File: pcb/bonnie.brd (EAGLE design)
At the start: 26.4 x 24.9 mm, 16 parts, among them J1 USB-MICROB, U1 MCP73831, U2 RT9013-XXXB

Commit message: fix: incorrect led oritentation
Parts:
- turned D3 to 0 degrees
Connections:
- net N$5: now also D3.C; no longer D3.A
- net VBUS: now also D3.A; no longer D3.C
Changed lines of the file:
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@@
 <attribute name="PROD_ID" value="RES-08295" x="46.355" y="40.005" size="1.778" layer="27" rot="R180" display="off"/>
 </element>
-<element name="D3" library="SparkFun-LED" package="LED-1206" value="RED" x="41.91" y="40.005" smashed="yes" rot="R180">
-<attribute name="PROD_ID" value="DIO-09912" x="41.91" y="40.005" size="1.778" layer="27" rot="R180" display="off"/>
-<attribute name="VALUE" x="42.926" y="41.783" size="0.4064" layer="27" rot="R180"/>
+<element name="D3" library="SparkFun-LED" package="LED-1206" value="RED" x="41.91" y="40.005" smashed="yes">
+<attribute name="PROD_ID" value="DIO-09912" x="41.91" y="40.005" size="1.778" layer="27" display="off"/>
+<attribute name="VALUE" x="40.894" y="38.227" size="0.4064" layer="27"/>
 </element>
 <element name="U2" library="v-reg-new" package="SOT23-5" value="RT9013-XXXB" x="34.925" y="36.195" smashed="yes">
@@
 <contactref element="U1" pad="4"/>
 <contactref element="C1" pad="2"/>
-<contactref element="D3" pad="C"/>
 <wire x1="45.2628" y1="35.6616" x2="45.0342" y2="35.6616" width="0.254" layer="1"/>
 <wire x1="45.0342" y1="35.6616" x2="43.434" y2="35.6616" width="0.254" layer="1"/>
 <wire x1="43.434" y1="35.6616" x2="43.395" y2="35.56" width="0.254" layer="1"/>
 <wire x1="45.2628" y1="35.6616" x2="45.405" y2="35.5299" width="0.254" layer="1"/>
-<wire x1="41.6052" y1="38.862" x2="40.4622" y2="40.005" width="0.254" layer="1"/>
+<wire x1="41.6052" y1="38.862" x2="40.8686" y2="39.5986" width="0.254" layer="1"/>
 <wire x1="41.6052" y1="36.576" x2="41.6052" y2="38.862" width="0.254" layer="16"/>
 <wire x1="40.6908" y1="35.6616" x2="41.6052" y2="36.576" width="0.254" layer="16"/>
@@
 <wire x1="42.9768" y1="35.2044" x2="42.9768" y2="34.29" width="0.254" layer="1"/>
 <wire x1="43.2054" y1="35.433" x2="42.9768" y2="35.2044" width="0.254" layer="1"/>
-<wire x1="40.4622" y1="40.005" x2="40.41" y2="40.005" width="0.254" layer="1"/>
 <wire x1="43.2054" y1="35.433" x2="43.395" y2="35.56" width="0.254" layer="1"/>
 <wire x1="45.0342" y1="35.6616" x2="45.0342" y2="33.8328" width="0.254" layer="1"/>
@@
 <via x="41.6052" y="38.862" extent="1-16" drill="0.6096"/>
 <via x="42.9768" y="34.29" extent="1-16" drill="0.6096"/>
+<contactref element="D3" pad="A"/>
+<wire x1="40.41" y1="40.005" x2="40.4622" y2="40.005" width="0.254" layer="1"/>
+<wire x1="40.4622" y1="40.005" x2="40.8686" y2="39.5986" width="0.254" layer="1"/>
 </signal>
 <signal name="N$1">
@@
 <signal name="N$5">
 <contactref element="R3" pad="2"/>
-<contactref element="D3" pad="A"/>
+<contactref element="D3" pad="C"/>
 <wire x1="43.41" y1="40.005" x2="45.505" y2="40.005" width="0.254" layer="1"/>
 </signal>

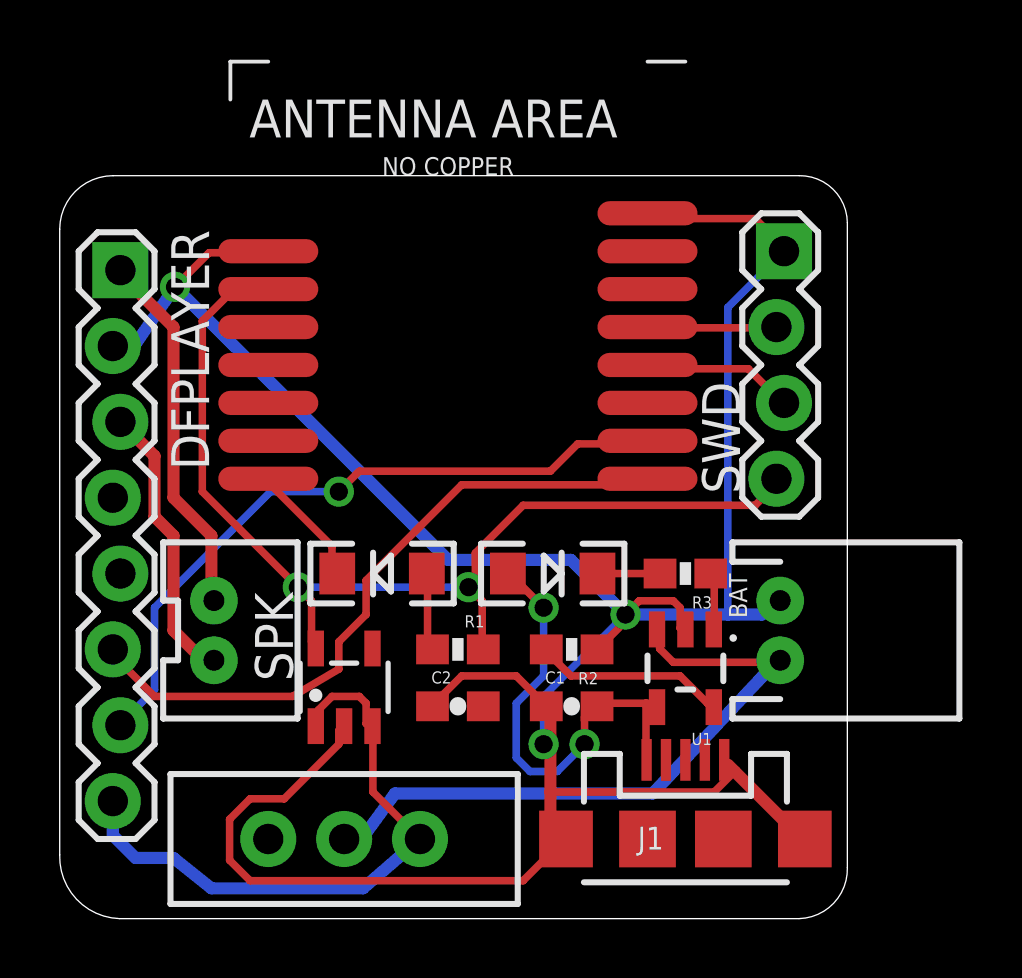
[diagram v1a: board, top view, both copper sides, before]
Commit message: switch to smaller package for LEDs (1206 -> 0603)
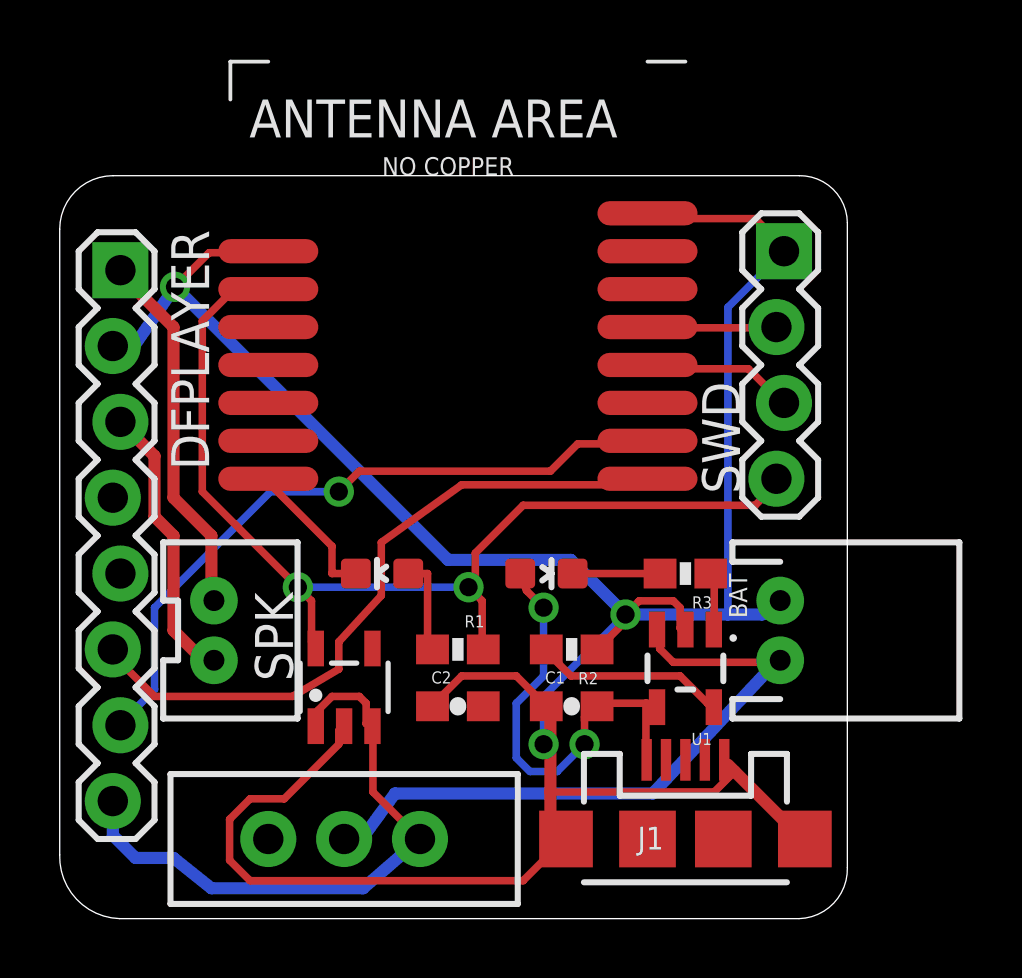
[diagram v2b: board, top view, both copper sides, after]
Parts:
- D2: value BLUE -> GREEN; device SparkFun-LED:LED-1206 -> SparkFun-LED:LED-0603
- D3: device SparkFun-LED:LED-1206 -> SparkFun-LED:LED-0603
- moved D3 0.21 mm to (41.7, 40.0), turned to 270 degrees
- turned D2 to 90 degrees
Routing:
- net N$5: track 2.10 -> 2.93 mm
- net N$3: track 4.22 -> 4.84 mm
- net N$2: track 2.71 -> 3.33 mm
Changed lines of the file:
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@@
 <layer number="220" name="220bmp" color="21" fill="1" visible="no" active="no"/>
 <layer number="221" name="221bmp" color="22" fill="1" visible="no" active="no"/>
+<layer number="222" name="222bmp" color="23" fill="1" visible="no" active="no"/>
 <layer number="223" name="223bmp" color="24" fill="1" visible="no" active="no"/>
 <layer number="224" name="224bmp" color="25" fill="1" visible="no" active="no"/>
@@
 <attribute name="VALUE" x="35.115" y="39.37" size="0.4064" layer="27" rot="R270"/>
 </element>
-<element name="D2" library="SparkFun-LED" package="LED-1206" value="BLUE" x="36.195" y="40.005" smashed="yes" rot="R180">
-<attribute name="PROD_ID" value="DIO-09912" x="36.195" y="40.005" size="1.778" layer="27" rot="R180" display="off"/>
-<attribute name="VALUE" x="37.211" y="41.783" size="0.4064" layer="27" rot="R180"/>
+<element name="D2" library="SparkFun-LED" package="LED-0603" value="GREEN" x="36.195" y="40.005" smashed="yes" rot="R90">
+<attribute name="PROD_ID" value="DIO-00821" x="36.195" y="40.005" size="1.778" layer="27" rot="R90" display="off"/>
+<attribute name="VALUE" value="GREEN" x="37.973" y="38.989" size="0.4064" layer="27" rot="R90"/>
 </element>
 <element name="R1" library="SparkFun-Resistors" package="0603-RES" value="4k7" x="38.735" y="37.465" smashed="yes" rot="R180">
@@
 <attribute name="PROD_ID" value="RES-08295" x="46.355" y="40.005" size="1.778" layer="27" rot="R180" display="off"/>
 </element>
-<element name="D3" library="SparkFun-LED" package="LED-1206" value="RED" x="41.91" y="40.005" smashed="yes">
-<attribute name="PROD_ID" value="DIO-09912" x="41.91" y="40.005" size="1.778" layer="27" display="off"/>
-<attribute name="VALUE" x="40.894" y="38.227" size="0.4064" layer="27"/>
+<element name="D3" library="SparkFun-LED" package="LED-0603" value="RED" x="41.7" y="40.005" smashed="yes" rot="R270">
+<attribute name="PROD_ID" value="DIO-00819" x="41.7" y="40.005" size="1.778" layer="27" rot="R270" display="off"/>
+<attribute name="VALUE" x="39.922" y="41.021" size="0.4064" layer="27" rot="R270"/>
 </element>
 <element name="U2" library="v-reg-new" package="SOT23-5" value="RT9013-XXXB" x="34.925" y="36.195" smashed="yes">
@@
 <contactref element="DFPLAYER" pad="6"/>
 <wire x1="38.862" y1="42.9768" x2="45.0342" y2="42.9768" width="0.254" layer="1"/>
-<wire x1="35.6616" y1="39.7764" x2="38.862" y2="42.9768" width="0.254" layer="1"/>
-<wire x1="35.6616" y1="38.6334" x2="35.6616" y2="39.7764" width="0.254" layer="1"/>
-<wire x1="34.7472" y1="37.719" x2="35.6616" y2="38.6334" width="0.254" layer="1"/>
+<wire x1="36.17" y1="41.0464" x2="38.862" y2="42.9768" width="0.254" layer="1"/>
+<wire x1="36.17" y1="39.2684" x2="36.17" y2="41.0464" width="0.254" layer="1"/>
+<wire x1="34.7472" y1="37.719" x2="36.17" y2="39.2684" width="0.254" layer="1"/>
 <wire x1="34.7472" y1="36.8046" x2="34.7472" y2="37.719" width="0.254" layer="1"/>
 <wire x1="33.1978" y1="35.8902" x2="34.7472" y2="36.8046" width="0.254" layer="1"/>
@@
 <wire x1="37.719" y1="40.005" x2="37.719" y2="37.4904" width="0.254" layer="1"/>
 <wire x1="37.719" y1="37.4904" x2="37.885" y2="37.465" width="0.254" layer="1"/>
-<wire x1="37.719" y1="40.005" x2="37.695" y2="40.005" width="0.254" layer="1"/>
+<wire x1="37.719" y1="40.005" x2="37.072" y2="40.005" width="0.254" layer="1"/>
 </signal>
 <signal name="N$3">
@@
 <wire x1="34.5186" y1="40.9194" x2="34.5186" y2="40.005" width="0.254" layer="1"/>
 <wire x1="32.4612" y1="42.9768" x2="34.5186" y2="40.9194" width="0.254" layer="1"/>
-<wire x1="34.5186" y1="40.005" x2="34.695" y2="40.005" width="0.254" layer="1"/>
+<wire x1="34.5186" y1="40.005" x2="35.318" y2="40.005" width="0.254" layer="1"/>
 <wire x1="32.4612" y1="42.9768" x2="32.385" y2="43.18" width="0.254" layer="1"/>
 </signal>
@@
 <wire x1="43.434" y1="35.6616" x2="43.395" y2="35.56" width="0.254" layer="1"/>
 <wire x1="45.2628" y1="35.6616" x2="45.405" y2="35.5299" width="0.254" layer="1"/>
-<wire x1="41.6052" y1="38.862" x2="40.8686" y2="39.5986" width="0.254" layer="1"/>
 <wire x1="41.6052" y1="36.576" x2="41.6052" y2="38.862" width="0.254" layer="16"/>
 <wire x1="40.6908" y1="35.6616" x2="41.6052" y2="36.576" width="0.254" layer="16"/>
@@
 <via x="42.9768" y="34.29" extent="1-16" drill="0.6096"/>
 <contactref element="D3" pad="A"/>
-<wire x1="40.41" y1="40.005" x2="40.4622" y2="40.005" width="0.254" layer="1"/>
-<wire x1="40.4622" y1="40.005" x2="40.8686" y2="39.5986" width="0.254" layer="1"/>
+<wire x1="40.823" y1="40.005" x2="41.033" y2="39.4342" width="0.254" layer="1"/>
+<wire x1="41.033" y1="39.4342" x2="41.6052" y2="38.862" width="0.254" layer="1"/>
 </signal>
 <signal name="N$1">
@@
 <contactref element="R3" pad="2"/>
 <contactref element="D3" pad="C"/>
-<wire x1="43.41" y1="40.005" x2="45.505" y2="40.005" width="0.254" layer="1"/>
+<wire x1="45.505" y1="40.005" x2="42.577" y2="40.005" width="0.254" layer="1"/>
 </signal>
 </signals>

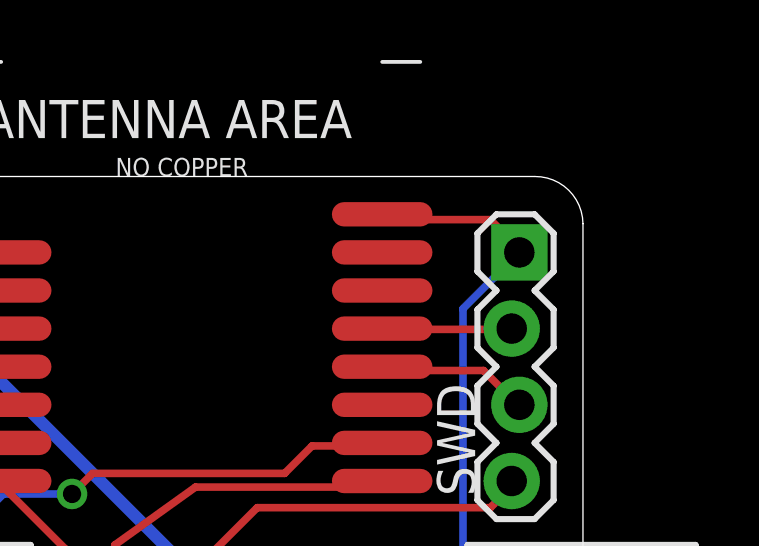
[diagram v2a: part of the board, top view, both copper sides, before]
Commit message: update board for PTR5618 module
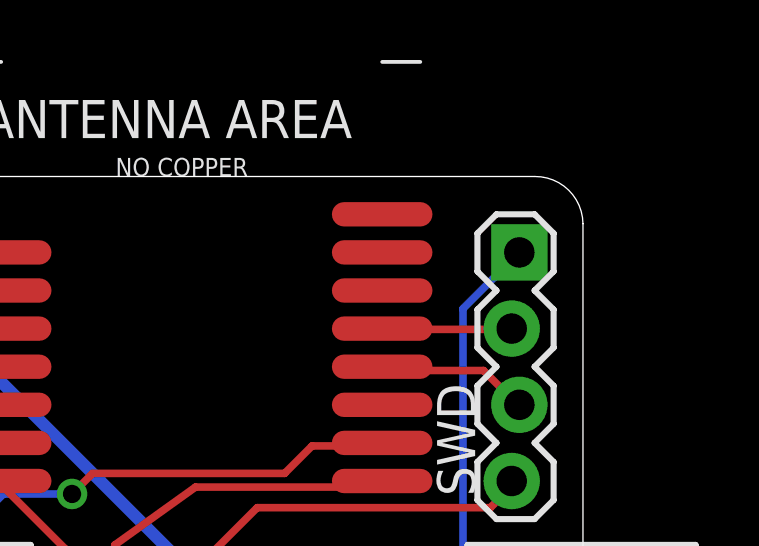
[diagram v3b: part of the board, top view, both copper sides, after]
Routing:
- net GND: track 98.9 -> 93.9 mm
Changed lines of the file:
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@@
 </signal>
 <signal name="GND">
-<contactref element="U$1" pad="8"/>
 <contactref element="SWD" pad="1"/>
 <contactref element="U$1" pad="9"/>
@@
 <wire x1="49.3776" y1="39.0906" x2="48.9204" y2="38.6334" width="0.4064" layer="16"/>
 <wire x1="49.3776" y1="39.0906" x2="49.53" y2="39.1" width="0.4064" layer="16"/>
-<wire x1="48.6918" y1="51.8922" x2="45.2628" y2="51.8922" width="0.254" layer="1"/>
-<wire x1="49.6062" y1="50.9778" x2="48.6918" y2="51.8922" width="0.254" layer="1"/>
-<wire x1="45.2628" y1="51.8922" x2="45.085" y2="52.07" width="0.254" layer="1"/>
+<wire x1="48.6918" y1="51.8922" x2="45.2628" y2="51.8922" width="0" layer="19" extent="1-16"/>
+<wire x1="49.6062" y1="50.9778" x2="48.6918" y2="51.8922" width="0" layer="19" extent="1-16"/>
 <wire x1="49.6062" y1="50.9778" x2="49.657" y2="50.8" width="0.254" layer="1"/>
 <wire x1="47.7774" y1="48.9204" x2="47.7774" y2="38.6334" width="0.254" layer="16"/>
@@
 <via x="44.3484" y="38.6334" extent="1-16" drill="0.6096"/>
 <via x="41.6052" y="34.29" extent="1-16" drill="0.6096"/>
+<contactref element="U$1" pad="8"/>
+<wire x1="45.2628" y1="51.8922" x2="45.085" y2="52.07" width="0" layer="19" extent="1-1"/>
 </signal>
 <signal name="SWCLK">
